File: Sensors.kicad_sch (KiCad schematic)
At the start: 19 parts, among them J300 Distance Sensor, U300 LIS2MDL, U301 LSM6DSL, U302 MS5607-02BA

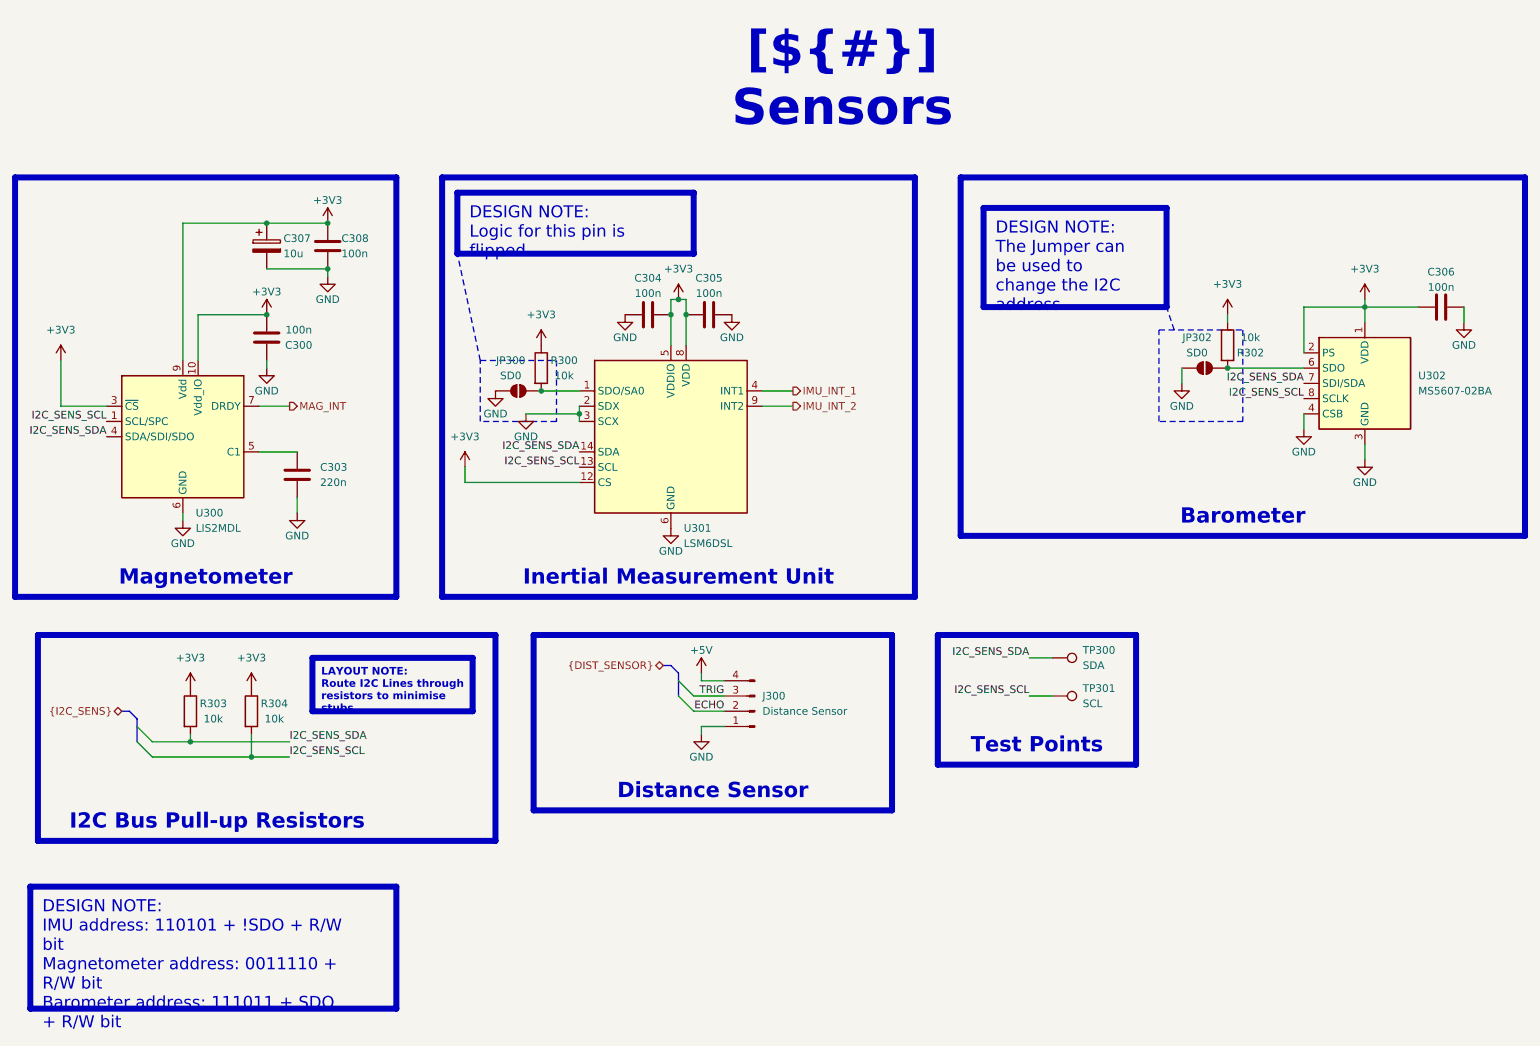
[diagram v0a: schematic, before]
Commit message: [pcb][changed] updated footprints that were incorrect, changed flash memory module due to stock issues
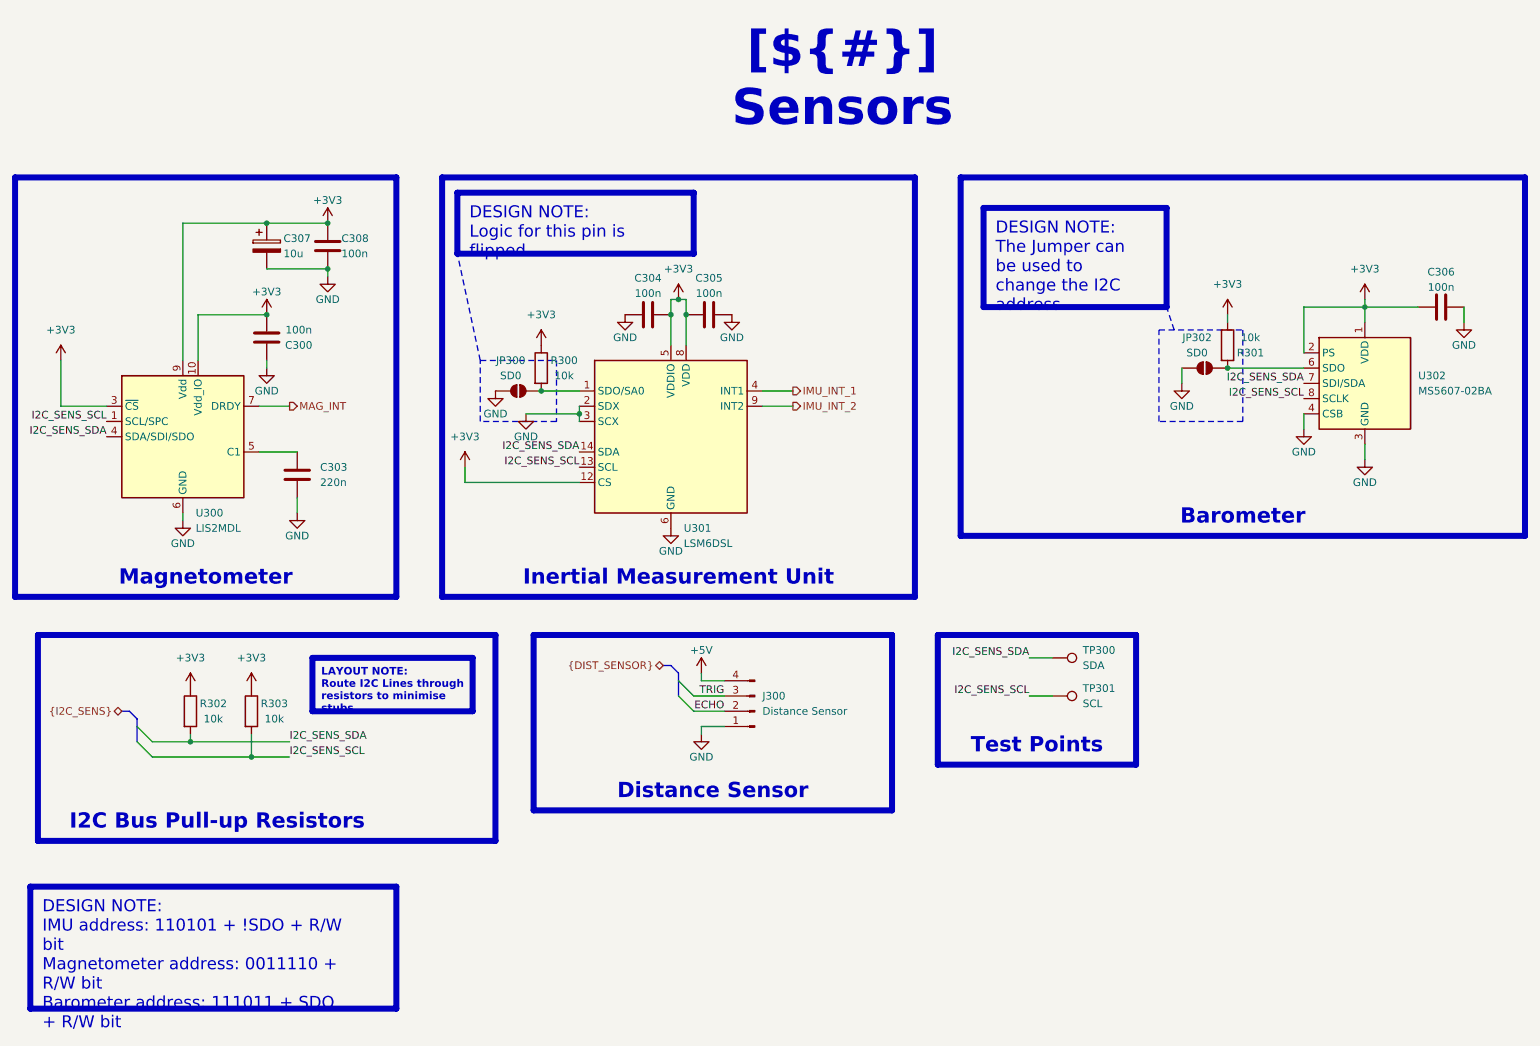
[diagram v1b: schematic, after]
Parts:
- renumbered R302 to R301, R303 to R302, R304 to R303
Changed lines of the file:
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@@
 		(on_board yes)
 		(dnp no)
-		(property "Reference" "R304"
+		(property "Reference" "R303"
 			(at 64.77 129.54 0)
 			(effects
@@
 			(project "DumbFCC"
 				(path "/f9e05184-c88b-4a88-ae9c-ab2bdb32be7c/c5103ceb-5325-4a84-a025-9638a412984e/e922dba6-6fdb-4354-bccd-57166a6199c3"
-					(reference "R304")
+					(reference "R303")
 					(unit 1)
 				)
@@
 		(on_board yes)
 		(dnp no)
-		(property "Reference" "R303"
+		(property "Reference" "R302"
 			(at 54.61 129.54 0)
 			(effects
@@
 			(project "DumbFCC"
 				(path "/f9e05184-c88b-4a88-ae9c-ab2bdb32be7c/c5103ceb-5325-4a84-a025-9638a412984e/e922dba6-6fdb-4354-bccd-57166a6199c3"
-					(reference "R303")
+					(reference "R302")
 					(unit 1)
 				)
@@
 		(on_board yes)
 		(dnp no)
-		(property "Reference" "R302"
+		(property "Reference" "R301"
 			(at 227.33 71.12 0)
 			(effects
@@
 			(project "DumbFCC"
 				(path "/f9e05184-c88b-4a88-ae9c-ab2bdb32be7c/c5103ceb-5325-4a84-a025-9638a412984e/e922dba6-6fdb-4354-bccd-57166a6199c3"
-					(reference "R302")
-					(unit 1)
-				)
+					(reference "R301")
+					(unit 1)
+				)
